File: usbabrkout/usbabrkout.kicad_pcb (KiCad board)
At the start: 4 copper layers, 27.7 x 20.3 mm, 12 parts, among them P101 CONN_01X01, P102 CONN_01X01, P103 CONN_01X01, P104 CONN_01X01, P105 USB_A

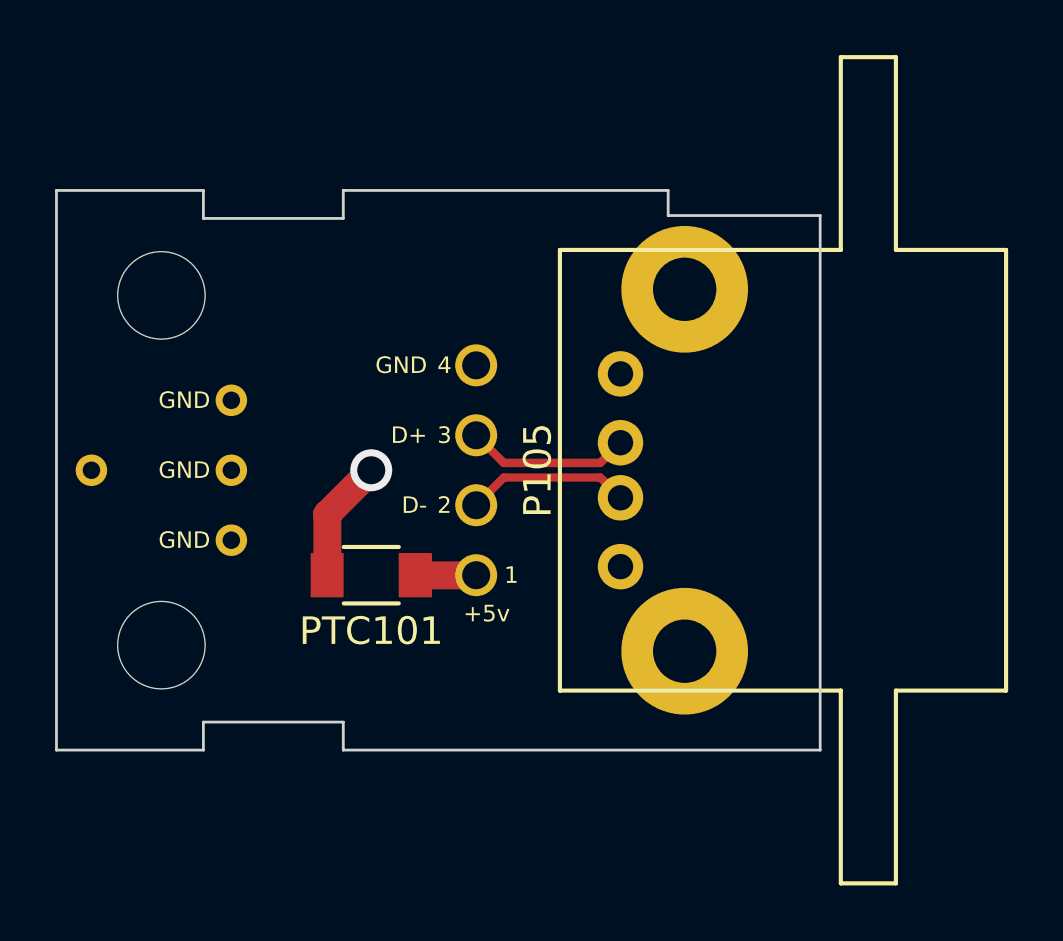
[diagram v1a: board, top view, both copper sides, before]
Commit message: Cleanup update to breakout boards. Upload to OSHpark.
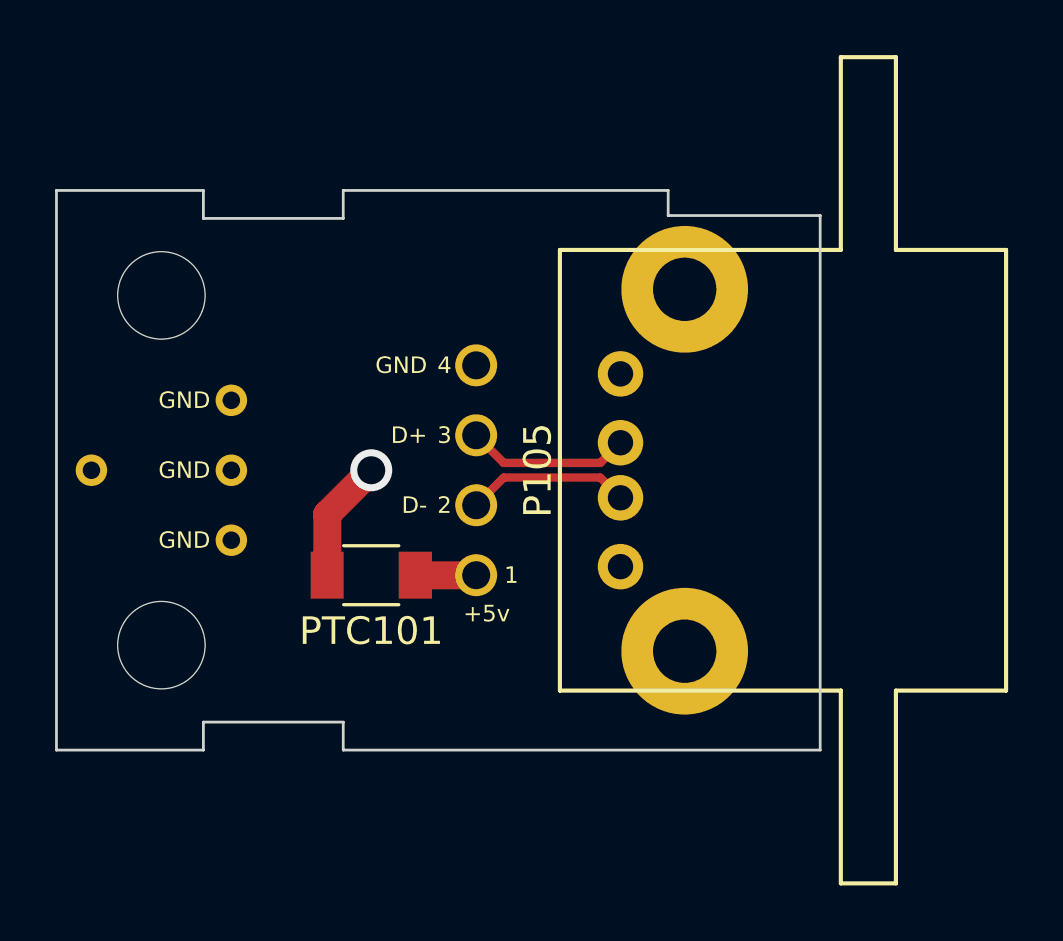
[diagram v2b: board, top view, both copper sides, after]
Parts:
- PTC101: footprint local:C_1206_HandSoldering -> local:R_1206_HandSoldering
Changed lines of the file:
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@@
     (links 11)
     (no_connects 0)
-    (area 128.219999 91.389999 156.050001 111.810001)
+    (area 120.619587 85.821253 163.078747 116.928747)
     (thickness 1.6)
     (drawings 39)
@@
       (net 1 GND))
   )
-  (module local:C_1206_HandSoldering (layer F.Cu)
+  (module local:R_1206_HandSoldering (layer F.Cu)
     (at 139.7 105.41)
-    (descr "Capacitor SMD 1206, hand soldering")
-    (tags "capacitor 1206")
+    (descr "Resistor SMD 1206, hand soldering")
+    (tags "resistor 1206")
     (attr smd)
     (fp_text reference PTC101 (at 0 2.032) (layer F.SilkS)
       (effects (font (size 1 1) (thickness 0.15)))
     )
-    (fp_text value 750mA (at 0 2.3) (layer F.Fab)
-      (effects (font (size 1 1) (thickness 0.15)))
-    )
-    (fp_line (start -2.5 -1.15) (end 2.5 -1.15) (layer F.CrtYd) (width 0.05))
-    (fp_line (start -2.5 1.15) (end 2.5 1.15) (layer F.CrtYd) (width 0.05))
-    (fp_line (start -2.5 -1.15) (end -2.5 1.15) (layer F.CrtYd) (width 0.05))
-    (fp_line (start 2.5 -1.15) (end 2.5 1.15) (layer F.CrtYd) (width 0.05))
-    (fp_line (start 1 -1.025) (end -1 -1.025) (layer F.SilkS) (width 0.15))
-    (fp_line (start -1 1.025) (end 1 1.025) (layer F.SilkS) (width 0.15))
-    (pad 1 smd rect (at -1.6 0) (size 1.2 1.6) (layers F.Cu F.Paste F.Mask)
+    (fp_text value 750mA (at 0 1.9) (layer F.Fab)
+      (effects (font (size 1 1) (thickness 0.15)))
+    )
+    (fp_text user %R (at 0 0) (layer F.Fab)
+      (effects (font (size 0.7 0.7) (thickness 0.105)))
+    )
+    (fp_line (start -1.6 0.8) (end -1.6 -0.8) (layer F.Fab) (width 0.1))
+    (fp_line (start 1.6 0.8) (end -1.6 0.8) (layer F.Fab) (width 0.1))
+    (fp_line (start 1.6 -0.8) (end 1.6 0.8) (layer F.Fab) (width 0.1))
+    (fp_line (start -1.6 -0.8) (end 1.6 -0.8) (layer F.Fab) (width 0.1))
+    (fp_line (start 1 1.07) (end -1 1.07) (layer F.SilkS) (width 0.12))
+    (fp_line (start -1 -1.07) (end 1 -1.07) (layer F.SilkS) (width 0.12))
+    (fp_line (start -3.25 -1.11) (end 3.25 -1.11) (layer F.CrtYd) (width 0.05))
+    (fp_line (start -3.25 -1.11) (end -3.25 1.1) (layer F.CrtYd) (width 0.05))
+    (fp_line (start 3.25 1.1) (end 3.25 -1.11) (layer F.CrtYd) (width 0.05))
+    (fp_line (start 3.25 1.1) (end -3.25 1.1) (layer F.CrtYd) (width 0.05))
+    (pad 1 smd rect (at -1.6 0) (size 1.2 1.7) (layers F.Cu F.Paste F.Mask)
       (net 4 VCC))
-    (pad 2 smd rect (at 1.6 0) (size 1.2 1.6) (layers F.Cu F.Paste F.Mask)
+    (pad 2 smd rect (at 1.6 0) (size 1.2 1.7) (layers F.Cu F.Paste F.Mask)
       (net 5 /+5v))
-    (model Capacitors_SMD.3dshapes/C_1206_HandSoldering.wrl
+    (model ${KISYS3DMOD}/Resistors_SMD.3dshapes/R_1206.wrl
       (at (xyz 0 0 0))
       (scale (xyz 1 1 1))
@@
   (gr_line (start 133.604 92.456) (end 138.684 92.456) (layer Edge.Cuts) (width 0.1))
   (gr_line (start 133.604 91.44) (end 133.604 92.456) (layer Edge.Cuts) (width 0.1))
-  (gr_text "USB-A Breakout" (at 142.748 93.345) (layer B.SilkS)
+  (gr_text "USB-A Breakout" (at 142.24 93.98) (layer B.SilkS)
     (effects (font (size 1 1) (thickness 0.15)) (justify mirror))
   )
-  (gr_text v1.0.0 (at 152.146 101.6) (layer B.SilkS)
+  (gr_text v1.0.0 (at 142.24 95.25) (layer B.SilkS)
     (effects (font (size 1 1) (thickness 0.15)) (justify mirror))
   )
-  (gr_text dcsun88osh@gmail.com (at 141.859 109.855) (layer B.SilkS)
+  (gr_text dcsun88osh@gmail.com (at 141.478 109.22) (layer B.SilkS)
     (effects (font (size 0.8 0.8) (thickness 0.15)) (justify mirror))
   )
@@
   (segment (start 148.016699 101.333301) (end 144.513301 101.333301) (width 0.3048) (layer F.Cu) (net 3))
   (segment (start 144.513301 101.333301) (end 143.51 100.33) (width 0.3048) (layer F.Cu) (net 3))
+  (segment (start 138.1 103.2) (end 138.1 105.41) (width 1.016) (layer F.Cu) (net 4))
   (segment (start 138.1 103.2) (end 139.7 101.6) (width 1.016) (layer F.Cu) (net 4))
   (via (at 139.7 101.6) (size 1.524) (drill 1.016) (layers F.Cu B.Cu) (net 4))
-  (segment (start 138.1 105.41) (end 138.1 103.2) (width 1.016) (layer F.Cu) (net 4))
-  (segment (start 143.51 105.41) (end 141.3 105.41) (width 1.016) (layer F.Cu) (net 5))
+  (segment (start 141.3 105.41) (end 143.51 105.41) (width 1.016) (layer F.Cu) (net 5))
   (zone (net 1) (net_name GND) (layer In1.Cu) (hatch edge 0.508)
     (connect_pads (clearance 0.253746))
